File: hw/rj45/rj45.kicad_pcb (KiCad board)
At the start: 4 copper layers, 62 x 11.8 mm, 17 parts, among them J1 SFP_Module_Edge, J2 RJ45, low profile - placehold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, T1 4-pair 1000BASE-T magnetics, 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, U1 DP83869HM, U2 STM32G031F6P6 (I2C slave: EEP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, U3 TPS62A01 3V3->1V1, U4 LDO 3V3->2V5, Y1 25 MHz

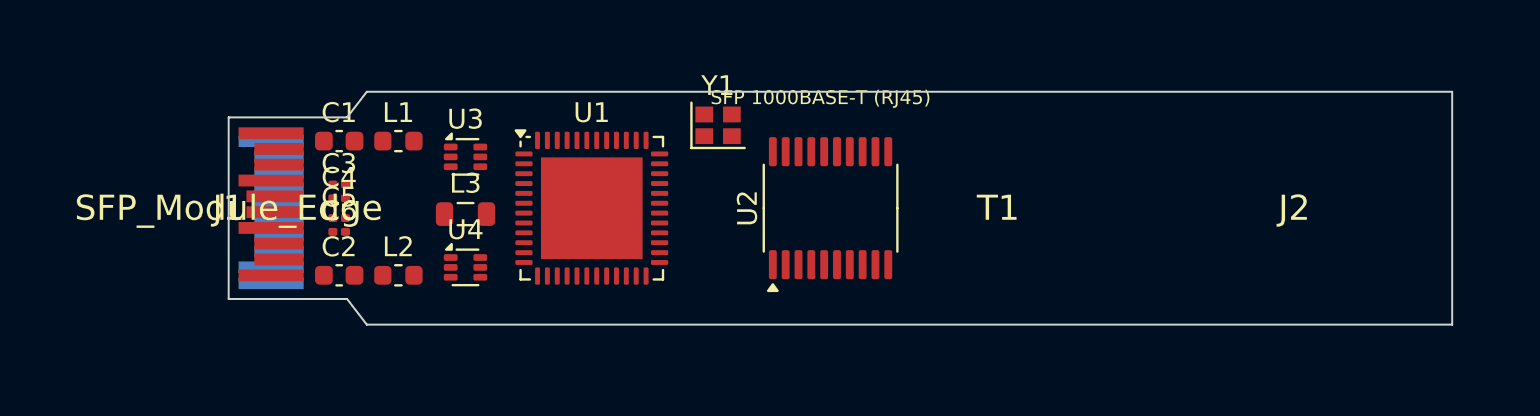
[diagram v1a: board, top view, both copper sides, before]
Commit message: RJ45: 6-layer board routed and clean, JLC panel and order sheet
- rj45: DRC 0 / 0 unconnected (KiCad 7 and 9), parity clean, ERC 0/0;
  gerbers, BOM/CPL, 1:1 print; 5-board panel with hand-placed tabs,
  checked with the board's own rules; ORDER.md with cost estimate
- sfpgen: side-pin power stubs clear the next pin's label (they shorted
  +3V3 to AVDD33 in the RJ45 schematic); project min via / hole clearance
  from the design
- t1: schematic regenerated with the stub fix, KiCad 9 re-checked
- CI: rj45 joins the KiCad 9 matrix
- t1s: work in progress (6 layers, not yet fully routed)
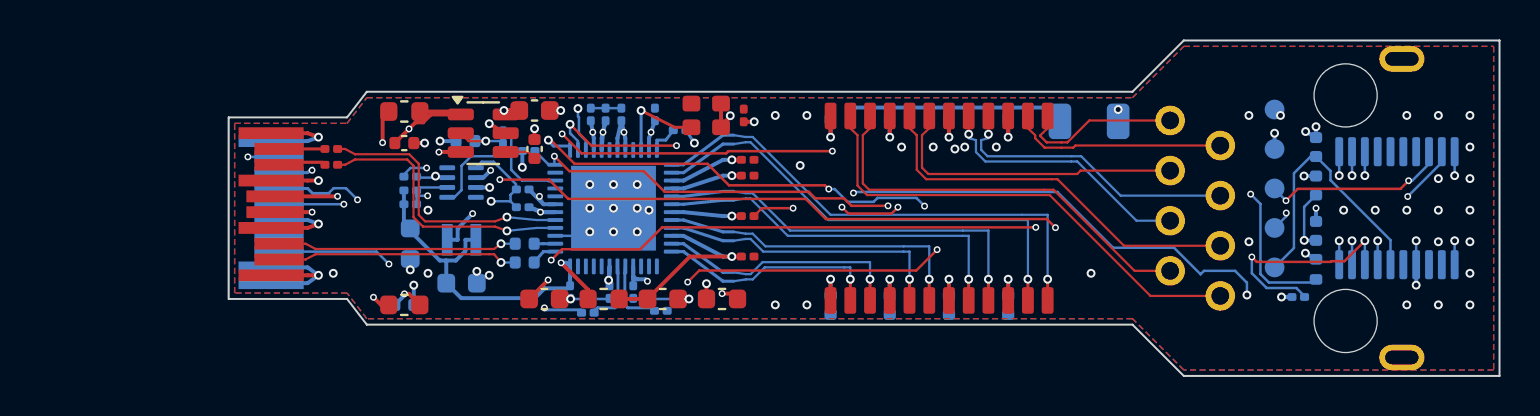
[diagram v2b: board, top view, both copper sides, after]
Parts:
- removed L2: ferrite VccR, L_0603_1608Metric
- removed L3: 1uH, L_0805_2012Metric
- removed Y1: 25 MHz, Crystal_SMD_2016-4Pin_2.0x1.6mm
- added C10: 100nF, Capacitor_SMD:C_0201_0603Metric, B.Cu at (121.6, 95.2)
- added C11: 100nF, Capacitor_SMD:C_0201_0603Metric, F.Cu at (126.3, 97.5)
- added C12: 100nF, Capacitor_SMD:C_0201_0603Metric, F.Cu at (126.3, 98.3)
- added C13: 100nF, Capacitor_SMD:C_0201_0603Metric, F.Cu at (126.3, 100.4)
- added C14: 100nF, Capacitor_SMD:C_0201_0603Metric, F.Cu at (126.3, 102.5)
- added C15: 100nF, Capacitor_SMD:C_0201_0603Metric, B.Cu at (120.5, 104.2)
- added C16: 100nF, Capacitor_SMD:C_0201_0603Metric, B.Cu at (119.3, 104.2)
- added C17: 100nF, Capacitor_SMD:C_0201_0603Metric, B.Cu at (117.3, 104.2)
- added C18: 100nF, Capacitor_SMD:C_0201_0603Metric, B.Cu at (114.9, 100.0)
- added C19: 100nF, Capacitor_SMD:C_0201_0603Metric, B.Cu at (114.9, 99.0)
- added C21: 10uF, Capacitor_SMD:C_0603_1608Metric, F.Cu at (122.0, 104.6)
- added C22: 10uF, Capacitor_SMD:C_0603_1608Metric, F.Cu at (116.0, 104.6)
- added C30: 100nF, Capacitor_SMD:C_0201_0603Metric, F.Cu at (126.1, 95.3)
- added C32: 4.7uF, Capacitor_SMD:C_0402_1005Metric, B.Cu at (112.0, 96.6)
- added C33: 10uF, Capacitor_SMD:C_0603_1608Metric, B.Cu at (109.2, 101.8)
- added C34: 10uF, Capacitor_SMD:C_0603_1608Metric, B.Cu at (111.8, 103.8)
- added C35: 120pF, Capacitor_SMD:C_0201_0603Metric, B.Cu at (109.2, 99.1)
- added C36: 100nF, Capacitor_SMD:C_0402_1005Metric, B.Cu at (130.5, 104.9)
- added C37: 100nF, Capacitor_SMD:C_0402_1005Metric, B.Cu at (133.5, 104.9)
- added C38: 100nF, Capacitor_SMD:C_0402_1005Metric, B.Cu at (136.5, 104.9)
- added C39: 100nF, Capacitor_SMD:C_0402_1005Metric, B.Cu at (139.5, 104.9)
- added C40: 1nF 2kV, Capacitor_SMD:C_1206_3216Metric, B.Cu at (143.6, 95.6)
- added C41: 100nF, Capacitor_SMD:C_0402_1005Metric, B.Cu at (155.1, 98.8)
- added C42: 1uF, Capacitor_SMD:C_0402_1005Metric, B.Cu at (155.1, 101.2)
- added C43: 100nF, Capacitor_SMD:C_0402_1005Metric, B.Cu at (155.1, 96.9)
- added C44: 2.2nF, Capacitor_SMD:C_0402_1005Metric, F.Cu at (115.5, 97.0)
- added C45: 10uF, Capacitor_SMD:C_0603_1608Metric, F.Cu at (115.5, 95.0)
- added C7: 100nF, Capacitor_SMD:C_0201_0603Metric, B.Cu at (118.3, 95.2)
- added C8: 100nF, Capacitor_SMD:C_0201_0603Metric, B.Cu at (119.1, 95.2)
- added C9: 100nF, Capacitor_SMD:C_0201_0603Metric, B.Cu at (119.9, 95.2)
- added FB1: BLM18KG601SH1, Inductor_SMD:L_0603_1608Metric, F.Cu at (108.9, 95.1)
- added FB2: BLM18KG601SH1, Inductor_SMD:L_0603_1608Metric, F.Cu at (108.9, 104.9)
- added FB3: BLM18KG601SH1, Inductor_SMD:L_0603_1608Metric, F.Cu at (119.0, 104.6)
- added FB4: BLM18KG601SH1, Inductor_SMD:L_0603_1608Metric, F.Cu at (125.0, 104.6)
- added R10: 1.5k, Resistor_SMD:R_0201_0603Metric, B.Cu at (154.2, 104.5)
- added R11: 4.7k, Resistor_SMD:R_0201_0603Metric, B.Cu at (115.2, 97.1)
- added R12: 4.7k, Resistor_SMD:R_0201_0603Metric, B.Cu at (121.9, 105.2)
- added R13: 4.7k, Resistor_SMD:R_0201_0603Metric, B.Cu at (118.2, 105.3)
- added R14: 75, Resistor_SMD:R_0402_1005Metric, B.Cu at (131.0, 95.5)
- added R15: 75, Resistor_SMD:R_0402_1005Metric, B.Cu at (134.0, 95.5)
- added R16: 75, Resistor_SMD:R_0402_1005Metric, B.Cu at (137.0, 95.5)
- added R17: 75, Resistor_SMD:R_0402_1005Metric, B.Cu at (140.0, 95.5)
- added R18: 100k, Resistor_SMD:R_0201_0603Metric, B.Cu at (113.9, 96.4)
- added R3: 57.6k 1%, Resistor_SMD:R_0201_0603Metric, B.Cu at (109.2, 99.8)
- added R4: 100k 1%, Resistor_SMD:R_0201_0603Metric, B.Cu at (109.2, 98.4)
- added R5: 10k, Resistor_SMD:R_0402_1005Metric, B.Cu at (155.1, 103.1)
- added R9: 2.49k 1%, Resistor_SMD:R_0201_0603Metric, B.Cu at (122.8, 96.0)
- added TP1: +3V3, TestPoint:TestPoint_Pad_D1.0mm, B.Cu at (153.0, 97.0)
- added TP2: SWDIO, TestPoint:TestPoint_Pad_D1.0mm, B.Cu at (153.0, 99.0)
- added TP3: SWCLK, TestPoint:TestPoint_Pad_D1.0mm, B.Cu at (153.0, 101.0)
- added TP4: NRST, TestPoint:TestPoint_Pad_D1.0mm, B.Cu at (153.0, 103.0)
- added TP5: GND, TestPoint:TestPoint_Pad_D1.0mm, B.Cu at (153.0, 95.0)
- added X1: MST8011AI-72-33E25, sfp:Oscillator_SMD_MST_2016-4Pin, F.Cu at (124.2, 95.3)
- C1: value 10uF VccT -> 1uF; footprint C_0603_1608Metric -> Capacitor_SMD:C_0402_1005Metric
- C2: value 10uF VccR -> 100nF; footprint C_0603_1608Metric -> Capacitor_SMD:C_0402_1005Metric; moved to B.Cu
- C3: value 100nF TD+ -> 100nF; footprint C_0201_0603Metric -> Capacitor_SMD:C_0201_0603Metric
- C4: value 100nF TD- -> 100nF; footprint C_0201_0603Metric -> Capacitor_SMD:C_0201_0603Metric
- C5: value 100nF RD+ -> 100nF; footprint C_0201_0603Metric -> Capacitor_SMD:C_0402_1005Metric; moved to B.Cu
- C6: value 100nF RD- -> 100nF; footprint C_0201_0603Metric -> Capacitor_SMD:C_0402_1005Metric; moved to B.Cu
- J1: value SFP_Module_Edge -> SFP edge (INF-8074i)
- J2: value RJ45, low profile - placeholder -> KH-RJ45-58-8P8C; footprint sfp:NOSE -> sfp:RJ45_Kinghelm_KH-RJ45-58
- L1: value ferrite VccT -> 470nH DFE201610E-R47M; footprint L_0603_1608Metric -> Inductor_SMD:L_Murata_DFE201610P; moved to B.Cu
- T1: value 4-pair 1000BASE-T magnetics, low profile - placeholder -> LP72450ANL; footprint sfp:MAG -> sfp:LINKPP_LP72450ANL
- U1: value DP83869HM -> RTL8221B-VB-CG; footprint QFN-48-1EP_7x7mm_P0.5mm_EP5.15x5.15mm -> Package_DFN_QFN:QFN-48-1EP_6x6mm_P0.4mm_EP4.3x4.3mm; moved to B.Cu
- U2: value STM32G031F6P6 (I2C slave: EEPROM A0/A2 + MDIO bridge 0x56) -> STM32G031F6P6; footprint TSSOP-20_4.4x6.5mm_P0.65mm -> Package_SO:TSSOP-20_4.4x6.5mm_P0.65mm; moved to B.Cu
- U3: value TPS62A01 3V3->1V1 -> TPS62822DLC; footprint SOT-563 -> sfp:Texas_VSON-HR-8_1.5x2mm_P0.5mm; moved to B.Cu
- U4: value LDO 3V3->2V5 -> TPS22918DBVR; footprint SOT-563 -> Package_TO_SOT_SMD:SOT-23-6
- moved U2 28.7 mm to (159.2, 100.0)
- moved J2 10.4 mm to (164.4, 100.0)
- moved C6 9.53 mm to (115.0, 102.8), turned to 180 degrees
- moved C5 9.49 mm to (115.0, 101.8), turned to 180 degrees
- moved U4 6.86 mm to (112.9, 96.2)
- moved L1 5.94 mm to (111.8, 101.6)
- moved C2 3.62 mm to (108.9, 104.9)
- moved C1 3.30 mm to (108.9, 96.7)
- moved T1 3.00 mm to (136.0, 100.0)
- moved C4 2.53 mm to (105.2, 97.0)
- moved U3 1.32 mm to (111.8, 98.7)
- moved U1 1.10 mm to (119.5, 100.0), turned to -90 degrees
- moved C3 1.08 mm to (105.2, 97.8)
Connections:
- C1 pad 1: (no net) -> VIN_RAW
- C1 pad 2: (no net) -> GND
- C2 pad 1: (no net) -> VIN_RAW
- C2 pad 2: (no net) -> GND
- C3 pad 1: (no net) -> TD_P
- C3 pad 2: (no net) -> HSI_P
- C4 pad 1: (no net) -> TD_N
- C4 pad 2: (no net) -> HSI_N
- C5 pad 1: (no net) -> HSO_P
- C5 pad 2: (no net) -> RD_P
- C6 pad 1: (no net) -> HSO_N
- C6 pad 2: (no net) -> RD_N
- J1 pad 1: (no net) -> GND
- J1 pad 10: (no net) -> GND
- J1 pad 11: (no net) -> GND
- J1 pad 12: (no net) -> RD_N
- J1 pad 13: (no net) -> RD_P
- J1 pad 14: (no net) -> GND
- J1 pad 15: (no net) -> VCCR
- J1 pad 16: (no net) -> VCCT
- J1 pad 17: (no net) -> GND
- J1 pad 18: (no net) -> TD_P
- J1 pad 19: (no net) -> TD_N
- J1 pad 2: (no net) -> TX_FAULT
- J1 pad 20: (no net) -> GND
- J1 pad 3: (no net) -> TX_DISABLE
- J1 pad 4: (no net) -> SDA
- J1 pad 5: (no net) -> SCL
- J1 pad 6: (no net) -> GND
- J1 pad 7: (no net) -> unconnected-(J1-RS0-Pad7)
- J1 pad 8: (no net) -> RX_LOS
- J1 pad 9: (no net) -> GND
- L1 pad 1: (no net) -> BUCK_SW
- L1 pad 2: (no net) -> V0P95
- U1 pad 1: (no net) -> PHY_RST_N
- U1 pad 10: (no net) -> XI
- U1 pad 11: (no net) -> AVDD09
- U1 pad 12: (no net) -> RSET
- U1 pad 13: (no net) -> MDI0_P
- U1 pad 14: (no net) -> MDI0_N
- U1 pad 15: (no net) -> AVDD33
- U1 pad 16: (no net) -> AVDD09
- U1 pad 17: (no net) -> MDI1_P
- U1 pad 18: (no net) -> MDI1_N
- U1 pad 19: (no net) -> AVDD33
- U1 pad 2: (no net) -> MDC
- U1 pad 20: (no net) -> MDI2_P
- U1 pad 21: (no net) -> MDI2_N
- U1 pad 22: (no net) -> AVDD09
- U1 pad 23: (no net) -> MDI3_P
- U1 pad 24: (no net) -> MDI3_N
- U1 pad 25: (no net) -> unconnected-(U1-SPISO-Pad25)
- U1 pad 26: (no net) -> unconnected-(U1-SPICSB-Pad26)
- U1 pad 27: (no net) -> unconnected-(U1-SPISCK-Pad27)
- U1 pad 28: (no net) -> V0P95
- U1 pad 29: (no net) -> CFG0
- U1 pad 3: (no net) -> MDIO
- U1 pad 30: (no net) -> CFG1
- U1 pad 31: (no net) -> +3V3
- U1 pad 32: (no net) -> unconnected-(U1-SPISI-Pad32)
- U1 pad 33: (no net) -> unconnected-(U1-LED0/PHYAD0-Pad33)
- U1 pad 34: (no net) -> unconnected-(U1-LED1/PHYAD1-Pad34)
- U1 pad 35: (no net) -> unconnected-(U1-LED2/PHYAD2-Pad35)
- U1 pad 36: (no net) -> V0P95
- U1 pad 37: (no net) -> HSO_N
- U1 pad 38: (no net) -> HSO_P
- U1 pad 39: (no net) -> GND
- U1 pad 4: (no net) -> V0P95
- U1 pad 40: (no net) -> HSI_P
- U1 pad 41: (no net) -> HSI_N
- U1 pad 42: (no net) -> +3V3
- U1 pad 43: (no net) -> V0P95
- U1 pad 44: (no net) -> unconnected-(U1-NC-Pad44)
- U1 pad 45: (no net) -> unconnected-(U1-NC-Pad45)
- U1 pad 46: (no net) -> BUCK_EN
- U1 pad 47: (no net) -> unconnected-(U1-NC-Pad47)
- U1 pad 48: (no net) -> PHY_INT_N
- U1 pad 49: (no net) -> GND
- U1 pad 5: (no net) -> +3V3
- U1 pad 6: (no net) -> unconnected-(U1-CLKOUT-Pad6)
- U1 pad 7: (no net) -> AVDD33
- U1 pad 8: (no net) -> AVDD33
- U1 pad 9: (no net) -> unconnected-(U1-CKXTAL2-Pad9)
- U2 pad 1: (no net) -> SDA
- U2 pad 10: (no net) -> PHY_INT_N
- U2 pad 11: (no net) -> TX_DISABLE
- U2 pad 12: (no net) -> RX_LOS
- U2 pad 13: (no net) -> TX_FAULT
- U2 pad 14: (no net) -> unconnected-(U2-PA7-Pad14)
- U2 pad 15: (no net) -> unconnected-(U2-PB0/PB1/PB2/PA8-Pad15)
- U2 pad 16: (no net) -> unconnected-(U2-PA11/PA9-Pad16)
- U2 pad 17: (no net) -> unconnected-(U2-PA12/PA10-Pad17)
- U2 pad 18: (no net) -> SWDIO
- U2 pad 19: (no net) -> SWCLK
- U2 pad 2: (no net) -> unconnected-(U2-PC14/PB9-Pad2)
- U2 pad 20: (no net) -> SCL
- U2 pad 3: (no net) -> unconnected-(U2-PC15-Pad3)
- U2 pad 4: (no net) -> +3V3
- U2 pad 5: (no net) -> GND
- U2 pad 6: (no net) -> NRST
- U2 pad 7: (no net) -> MDC
- U2 pad 8: (no net) -> MDIO
- U2 pad 9: (no net) -> PHY_RST_N
- U3 pad 1: (no net) -> BUCK_EN
- U3 pad 2: (no net) -> BUCK_FB
- U3 pad 3: (no net) -> GND
- U3 pad 4: (no net) -> unconnected-(U3-NC-Pad4)
- U3 pad 5: (no net) -> GND
- U3 pad 6: (no net) -> BUCK_SW
- U4 pad 1: (no net) -> VIN_RAW
- U4 pad 2: (no net) -> GND
- U4 pad 3: (no net) -> VIN_RAW
- U4 pad 4: (no net) -> SS_CT
- U4 pad 5: (no net) -> +3V3
- U4 pad 6: (no net) -> +3V3
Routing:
- net TX_DISABLE: track 0.00 -> 74.3 mm, vias 0 -> 5
- net SDA: track 0.00 -> 73.5 mm, vias 0 -> 4
- net SCL: track 0.00 -> 72.1 mm, vias 0 -> 4
- net RX_LOS: track 0.00 -> 70.1 mm, vias 0 -> 4
- net TX_FAULT: track 0.00 -> 64.6 mm, vias 0 -> 4
- net MDIO: track 0.00 -> 60.7 mm, vias 0 -> 3
- net MDC: track 0.00 -> 50.6 mm, vias 0 -> 5
- net PHY_RST_N: track 0.00 -> 48.9 mm, vias 0 -> 4
- net PHY_INT_N: track 0.00 -> 47.6 mm, vias 0 -> 3
- net GND: track 0.00 -> 47.0 mm, vias 0 -> 66
- net V0P95: track 0.00 -> 37.7 mm, vias 0 -> 4
- net AVDD33: track 0.00 -> 35.1 mm, vias 0 -> 5
- net AVDD09: track 0.00 -> 26.6 mm, vias 0 -> 3
- net MDI0_P: track 0.00 -> 25.5 mm, vias 0 -> 1
- net LINE0_P: track 0.00 -> 24.4 mm
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- added copper zone on In3.Cu, net +3V3
- added copper zone on B.Cu, net GND
- added copper zone on F.Cu, net GND
- added copper zone on In1.Cu, net GND
- added copper zone on In4.Cu, net GND
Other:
- board size 62 x 11.8 mm -> 64.4 x 17 mm
- copper layers 4 -> 6
- board text added: "RJ45 SFP"
- board text removed: "SFP 1000BASE-T (RJ45)"
- board text removed: "inside cage: top <= 4.65 mm, bottom <= 1.65 mm"

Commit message: References checked against the design; the fixes they turned up
docs/REFERENCES.md: the standards, Linux drivers, TI / Realtek / Microchip /
Gowin datasheets, app notes and EVMs, and commercial modules, each with a
table of the design against it.

Fixed from it:
- T1S: CLKHOLD_N (K3) tied high - pulled down during configuration, it would
  have held the flash clock and the FPGA would never load; P1 (also
  SSPI_CS_N) pulled up (R26); AN1718 BIN: 0.75 W end-node resistors (were
  0.25 W), 100 V centre cap (was 50 V), no copper under the CMC
- RJ45 / T1S: buck inductor 1.0 uH (TPS6282x Table 3): the RTL8221B wants
  its core switcher out of pulse skipping, which now starts at ~0.15 A, not
  ~0.33 A
- T1: no copper under the CMC on F/In1 (DP83TG720 8.5); the TC812 loadout
  fits the 200 uH CMC its datasheet asks for
- fw: PHY settings 70 ms after reset release (TG720: 65 ms before the first
  MDIO frame) with the 0x56 bridge answering 0xFFFF until then; LAN8670 set-up
  picked by silicon revision (AN1699 Rev G: C2 or D0); collision detection
  follows PLCA as AN1699 asks

All three boards: DRC 0 / 0 unconnected, KiCad 9 PASS, panels clean.
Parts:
- L1: value 470nH DFE201610E-R47M -> 1uH DFE201610E-1R0M
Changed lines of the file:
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@@
     (descr "Inductor, Murata, DFE201610P, 2.0x1.6x1.0mm, https://www.murata.com/~/media/webrenewal/products/inductor/chip/tokoproducts/wirewoundmetalalloychiptype/m_dfe201610p.ashx")
     (tags "Inductor power chip flatwire")
-    (property "LCSC" "C269773")
+    (property "LCSC" "C161082")
     (property "Sheetfile" "rj45.kicad_sch")
     (property "Sheetname" "")
@@
         (effects (font (size 1 1) (thickness 0.15)) (justify mirror))
     )
-    (fp_text value "470nH DFE201610E-R47M" (at 0 -1.8 180) (layer "B.Fab") hide
+    (fp_text value "1uH DFE201610E-1R0M" (at 0 -1.8 180) (layer "B.Fab") hide
         (effects (font (size 1 1) (thickness 0.15)) (justify mirror))
     )

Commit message: RJ45 re-laid on the corrected SFP edge: U1 on top
With the edge drawn the right way round (SFF-8419 Figure 7-2) the RTL8221B's
SerDes pins meet RD-, RD+, TD+, TD- straight only from the top side; it has
no SerDes polarity swap. U1's group (decaps, straps, fan, oscillator, analog
beads, HSO caps) is turned over as one body in make_rj45.py; the links to
the rest are laid new:
- HSI and RD pairs on top, P to P, no via
- MDI on top under the magnetics' body straight into the chip-side pads,
  port 0 on channel 1; CFG_OPT1 now pulled down (no MDI swap)
- the slow lines laid on In2 end to end in the jack bus's lane order; the
  MCU's GPIOs follow it (fw VARIANT_RJ45: PA0 MDIO, PA1 MDC, PA4 TX_FAULT,
  PA5 TX_DISABLE, PA6 RX_LOS)
- both VCC beads, the load switch and its caps below the HSI pair; the
  buck's switch node under its own body; panel tabs moved off U4 and X1
DRC 0 / 0 unconnected, ERC 0, KiCad 9 PASS, panel 0 errors. T1S still
carries the mirrored edge.
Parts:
- C1, C11, C12, C13, C14, C21, C22, C30, C45, FB3, FB4, X1: moved to B.Cu
- C10, C15, C16, C17, C18, C19, C5, C6, C7, C8, C9, R12, R13, R9, U1: moved to F.Cu
- moved R13 10.6 mm to (118.2, 94.7)
- moved R12 10.4 mm to (121.9, 94.8)
- moved FB1 9.80 mm to (108.9, 104.9)
- moved C45 9.55 mm to (115.7, 104.6)
- moved C10 9.50 mm to (121.6, 104.8), turned to -90 degrees
- moved C7 9.50 mm to (118.3, 104.8), turned to -90 degrees
- moved C8 9.50 mm to (119.1, 104.8), turned to -90 degrees
- moved C9 9.50 mm to (119.9, 104.8), turned to -90 degrees
- moved C30 9.40 mm to (126.1, 104.7), turned to -90 degrees
- moved X1 9.40 mm to (124.2, 104.7)
- moved C21 9.20 mm to (122.0, 95.4)
- moved C22 9.20 mm to (116.0, 95.4)
- moved FB3 9.20 mm to (119.0, 95.4)
- moved FB4 9.20 mm to (125.0, 95.4)
- moved C1 8.71 mm to (111.0, 105.2)
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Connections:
- R13 pad 1: +3V3 -> GND
- T1 pad 11: MDI0_N -> MDI3_P
- T1 pad 12: MDI0_P -> MDI3_N
- T1 pad 2: MDI3_N -> MDI0_P
- T1 pad 3: MDI3_P -> MDI0_N
- T1 pad 5: MDI2_N -> MDI1_P
- T1 pad 6: MDI2_P -> MDI1_N
- T1 pad 8: MDI1_N -> MDI2_P
- T1 pad 9: MDI1_P -> MDI2_N
- U2 pad 11: TX_DISABLE -> TX_FAULT
- U2 pad 12: RX_LOS -> TX_DISABLE
- U2 pad 13: TX_FAULT -> RX_LOS
- U2 pad 7: MDC -> MDIO
- U2 pad 8: MDIO -> MDC
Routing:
- net +3V3: track 23.8 -> 43.7 mm, vias 19 -> 18
- net MDI3_N: track 11.5 -> 25.5 mm, vias 1 -> 0
- net MDI0_P: track 25.5 -> 11.5 mm, vias 1 -> 0
- net MDI3_P: track 12.7 -> 24.2 mm, vias 1 -> 0
- net MDI0_N: track 24.2 -> 12.7 mm, vias 1 -> 0
- net SDA: track 73.5 -> 63.1 mm, vias 4 -> 2
- net VIN_RAW: track 19.0 -> 8.90 mm, vias 3 -> 2
- net RX_LOS: track 70.1 -> 60.4 mm, vias 4 -> 2
- net MDIO: track 60.7 -> 51.7 mm, vias 3 -> 4
- net SCL: track 72.1 -> 63.1 mm, vias 4 -> 2
- net MDI2_N: track 14.9 -> 20.8 mm, vias 1 -> 0
- net PHY_INT_N: track 47.6 -> 53.5 mm
- net AVDD33: track 35.1 -> 40.6 mm
- net MDI1_P: track 20.4 -> 15.1 mm, vias 1 -> 0
- net MDC: track 50.6 -> 45.5 mm, vias 5 -> 2
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
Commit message: RJ45: PHY address straps on LED0/1/2, re-routed: DRC 0 / 0, KiCad 9 PASS, panel 0 errors
The RTL8221B's CONFIG pins have no internal pulls (datasheet 7.18), so
LED0/1/2 (PHYAD[2:0]) floated. R19-R21, 4.7k to ground: PHYAD 000, which the
PHY maps to address 1 (Table 16 note 2), the firmware's address. Three 0201s
above pins 33-35; C16 moved underneath its via, C17 0.3 mm west.

R11 (INT's pull-up) moved under INT's In2 via. Two links the router left
open are laid by hand before routing (VCCR finger to FB2 through In2, R4's
feedback end through In2); one fresh Freerouting session around them is
kept as rj45.ses.

sfpgen, for board rebuilds:
- plane_dogbones' no-room fallback no longer lays a pad-centre copy of a
  link the pad already has through hand-laid copper (it ran a +3V3 stub
  into the edge strip, and the n <= n0 DRC count let it through);
- drop_duplicate_plane_vias also drops GND router vias inside a locked GND
  via, and the later of two locked same-net vias on top of each other.

KiCad 7 DRC 0 / 0 unconnected, ERC 0; KiCad 9 DRC 0 errors, parity clean,
ERC 0 errors; panel 0 errors, 0 unconnected; edge pins as SFF-8419.
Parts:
- added R19: 4.7k, Resistor_SMD:R_0201_0603Metric, F.Cu at (118.7, 95.9)
- added R20: 4.7k, Resistor_SMD:R_0201_0603Metric, F.Cu at (118.2, 95.9)
- added R21: 4.7k, Resistor_SMD:R_0201_0603Metric, F.Cu at (117.6, 95.9)
- C16: moved to B.Cu
- moved R11 6.00 mm to (115.2, 103.1)
- moved C16 1.10 mm to (119.3, 96.8), turned to -90 degrees
- moved C17 0.30 mm to (117.0, 95.8)
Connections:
- U1 pad 33: unconnected-(U1-LED0/PHYAD0-Pad33) -> LED0
- U1 pad 34: unconnected-(U1-LED1/PHYAD1-Pad34) -> LED1
- U1 pad 35: unconnected-(U1-LED2/PHYAD2-Pad35) -> LED2
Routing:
- net PHY_INT_N: track 53.5 -> 46.1 mm, vias 3 -> 2
- net +3V3: track 43.7 -> 40.1 mm
- net GND: track 45.3 -> 42.8 mm
- net NRST: track 14.0 -> 16.2 mm
- net AVDD33: track 40.6 -> 42.4 mm
- net VIN_RAW: track 8.90 -> 10.6 mm
- net V0P95: track 36.3 -> 34.8 mm
- net LED2: track 0.00 -> 1.12 mm
- net BUCK_EN: track 12.6 -> 13.6 mm
- net LED0: track 0.00 -> 0.99 mm
- net LED1: track 0.00 -> 0.94 mm
- net SWCLK: track 11.6 -> 10.7 mm
- net VCCT: track 11.5 -> 10.7 mm
